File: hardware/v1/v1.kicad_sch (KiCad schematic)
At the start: 27 parts, among them J1 FPC 24P 0.5mm bottom contact, J2 UP port, JST-SH 4, J3 DN port, JST-SH 4, J4 UP, magnetic pogo pins, Q1 AO3400A, SW1 power, SW2 A: next, SW3 B: confirm, U1 Raspberry Pi Pico 2 (no heade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

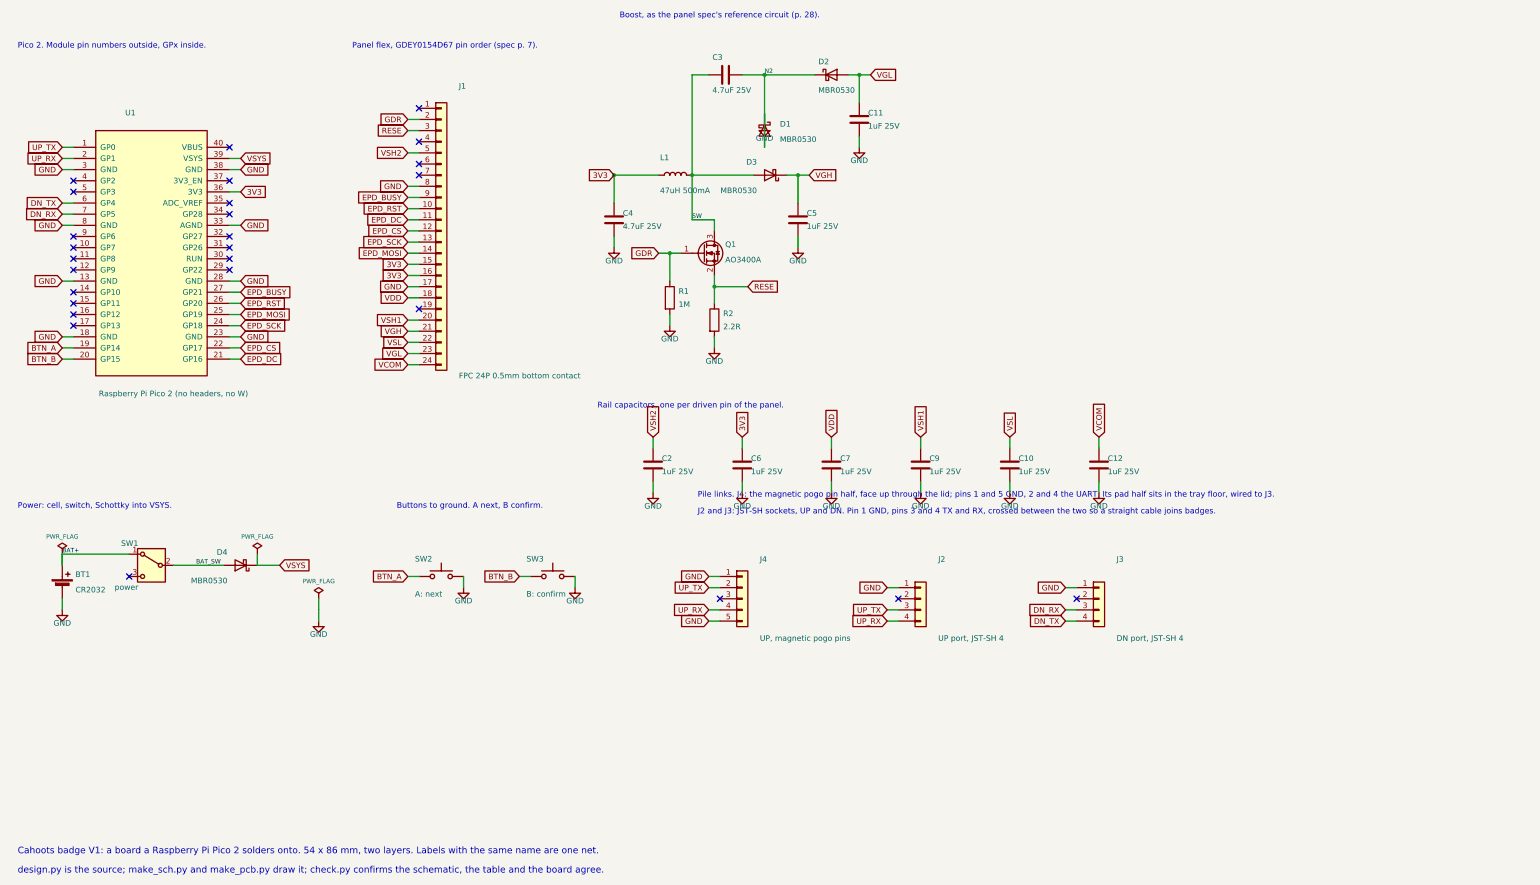
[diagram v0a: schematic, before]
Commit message: V1: regenerated with J5 (Qwiic, bottom centre) and J6 (2x5 header, back at -5,-30); 0 incomplete, 0 DRC; render scripts use web/ for Playwright
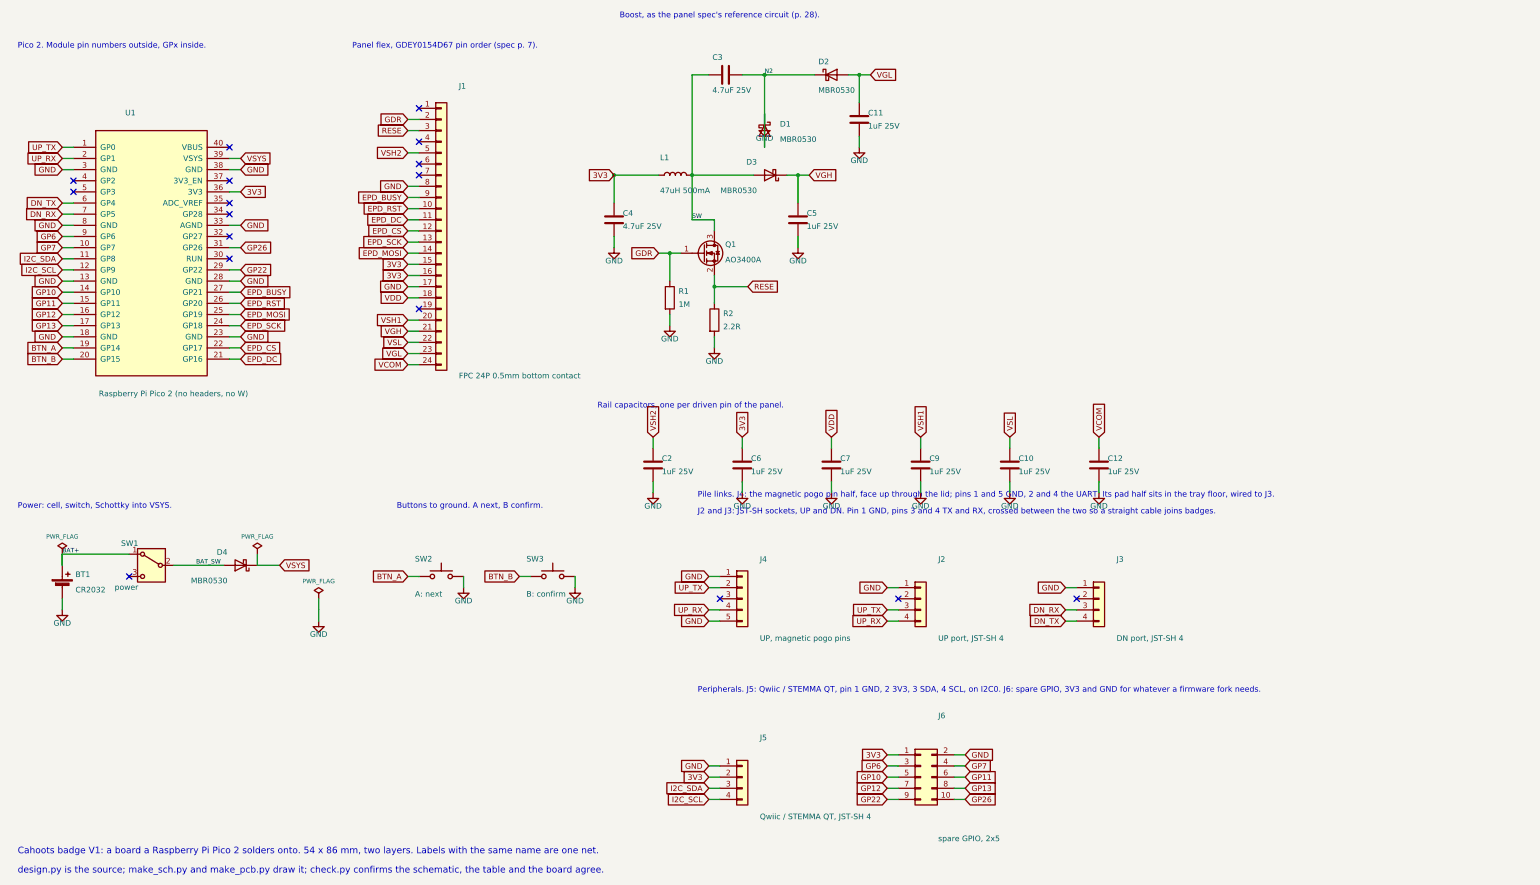
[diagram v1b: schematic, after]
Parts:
- added J5: Qwiic / STEMMA QT, JST-SH 4, Connector_JST:JST_SH_SM04B-SRSS-TB_1x04-1MP_P1.00mm_Horizontal, symbol Connector_Generic:Conn_01x04
- added J6: spare GPIO, 2x5, Connector_PinHeader_2.54mm:PinHeader_2x05_P2.54mm_Vertical, symbol Connector_Generic:Conn_02x05_Odd_Even
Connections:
- net 3V3: now also J5.2 (Pin_2), J6.1 (Pin_1)
- net GND: now also J5.1 (Pin_1), J6.2 (Pin_2)
- net GP7: now reaches U1.10 (GP7)
- net GP7: now also J6.4 (Pin_4)
- net I2C_SDA: now reaches U1.11 (GP8)
- net I2C_SDA: now also J5.3 (Pin_3)
- net I2C_SCL: now reaches U1.12 (GP9)
- net I2C_SCL: now also J5.4 (Pin_4)
- net GP10: now reaches U1.14 (GP10)
- net GP10: now also J6.5 (Pin_5)
- net GP11: now reaches U1.15 (GP11)
- net GP11: now also J6.6 (Pin_6)
- net GP12: now reaches U1.16 (GP12)
- net GP12: now also J6.7 (Pin_7)
- net GP13: now reaches U1.17 (GP13)
- net GP13: now also J6.8 (Pin_8)
- net GP22: now reaches U1.29 (GP22)
- net GP22: now also J6.9 (Pin_9)
- net GP26: now reaches U1.31 (GP26)
- net GP26: now also J6.10 (Pin_10)
- net GP6: now reaches U1.9 (GP6)
- net GP6: now also J6.3 (Pin_3)
- no-connect marks 27 -> 17
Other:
- note added: "Peripherals. J5: Qwiic / STEMMA QT, pin 1 GND, 2 3V3, 3 SDA, 4 SCL, on I2C0. J6: spare GPIO, 3V3 and GND for whatever a firmware fork needs."
